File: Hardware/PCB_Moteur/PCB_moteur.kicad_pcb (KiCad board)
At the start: 2 copper layers, 60 x 113 mm, 191 parts, among them J1 XT30PW-F, J10 Conn_01x02, J11 Conn_01x02, J12 Conn_01x02, J13 Conn_01x02, J14 Conn_01x02, J15 Conn_01x02, J16 Conn_01x06_Pin, J17 Screw_Terminal_01x04, J18 Screw_Terminal_01x04, J19 Screw_Terminal_01x04, J2 Conn_01x06_Pin, J3 Conn_01x03_Socket, J4 Conn_01x03_Socket, J5 Conn_01x03_Socket, J6 Conn_01x03_Socket, J7 Conn_01x02, J8 Conn_01x02, J9 Conn_01x02, Q1 SI5442DU-T1-GE3, Q2 SI5442DU-T1-GE3, Q3 MMBT3904, Q4 SI7617DN-T1-GE3, U1 L6981N33DR, U2 STM32F103CBT6, U3 MCP1802T-5002I/OT, U4 LSF0204PWR, U5 ISOW1044, U6 LM393, U7 INA125UA/2K5, U8 INA125UA/2K5, U9 MAX6612MXK

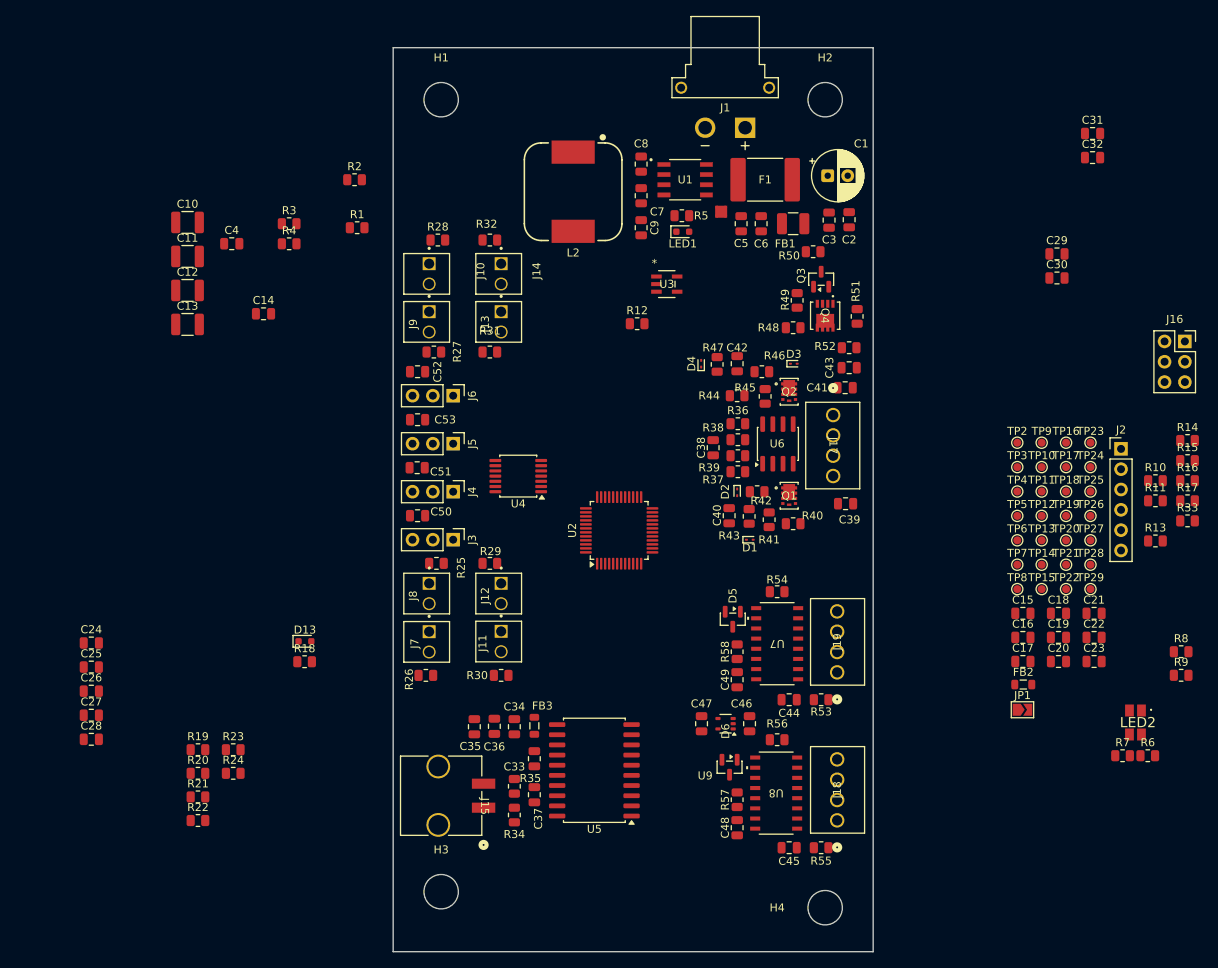
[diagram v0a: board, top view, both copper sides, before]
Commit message: wip: layout presque fini (decoup stm32 restant)
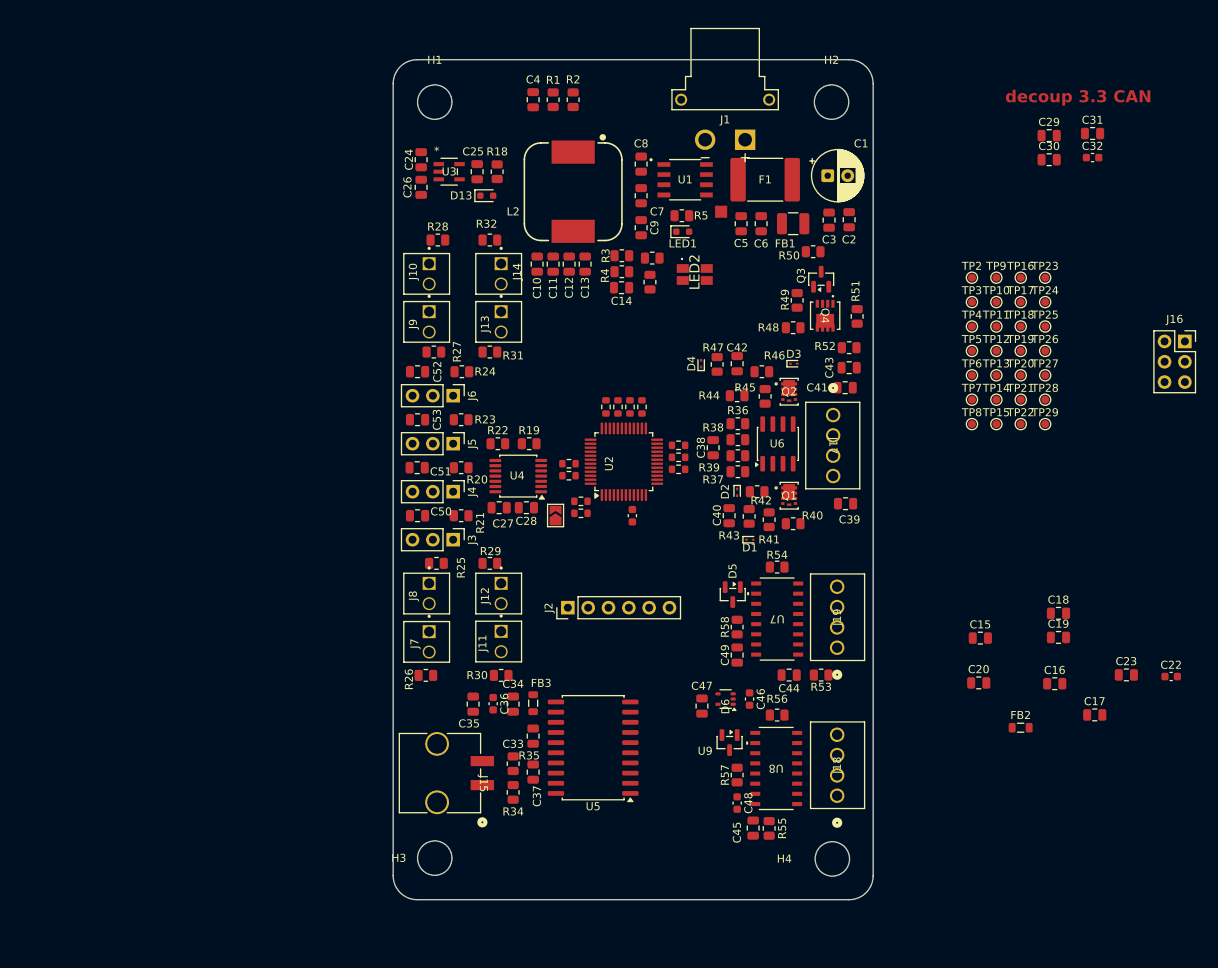
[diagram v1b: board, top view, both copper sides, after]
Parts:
- C10, C11, C12, C13: footprint Capacitor_SMD:C_1210_3225Metric -> Capacitor_SMD:C_0805_2012Metric
- C21, C22, C32, C36, C46, C48: footprint Capacitor_SMD:C_0805_2012Metric -> Capacitor_SMD:C_0603_1608Metric
- R10, R11, R12, R13, R14, R15, R16, R17, R33, R8, R9: footprint Resistor_SMD:R_0805_2012Metric -> Resistor_SMD:R_0603_1608Metric
- moved R6 87.8 mm to (115.4, 59.3)
- moved R7 83.6 mm to (115.1, 62.3), turned to 90 degrees
- moved LED2 78.6 mm to (120.7, 61.4), turned to 90 degrees
- moved C25 78.5 mm to (93.5, 48.5), turned to -90 degrees
- moved R9 78.1 mm to (106.5, 89.7)
- moved R33 77.6 mm to (105.0, 85.0)
- moved R8 77.0 mm to (106.5, 91.2), turned to 180 degrees
- moved C26 75.3 mm to (86.5, 50.5), turned to 90 degrees
- moved R13 73.8 mm to (105.0, 86.5)
- moved R17 73.6 mm to (109.6, 77.9), turned to 90 degrees
- moved C24 73.1 mm to (86.5, 47.0), turned to -90 degrees
- moved J2 71.9 mm to (104.8, 103.0), turned to 90 degrees
- moved R16 71.8 mm to (111.1, 77.9), turned to 90 degrees
- moved R15 70.0 mm to (112.6, 77.9), turned to 90 degrees
- moved R14 68.3 mm to (114.1, 77.9), turned to 90 degrees
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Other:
- board size 60 x 113 mm -> 60 x 105 mm
- board text added: "decoup 3.3 CAN"

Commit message: wip: nouveaux connecteurs et espace pour ceux-ci
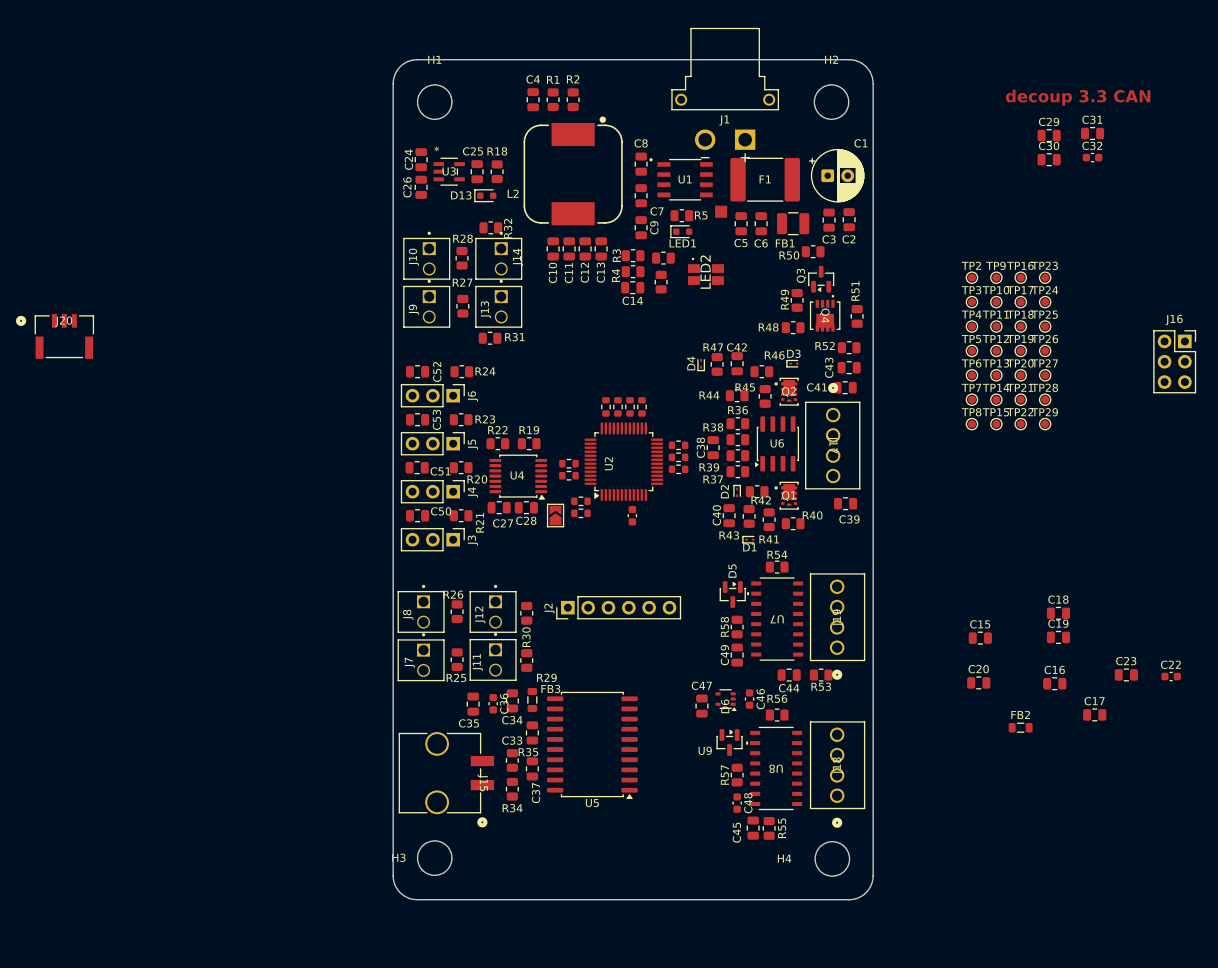
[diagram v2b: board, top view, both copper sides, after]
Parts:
- added J20: BM03B-GHS-TBT, pcb_moteur:CONN_BM03B-GHS-TBT_JST, F.Cu at (41.9, 69.1)
- moved R29 13.0 mm to (99.7, 109.6), turned to -90 degrees
- moved R25 12.3 mm to (91.0, 109.5), turned to -90 degrees
- moved R26 8.87 mm to (91.0, 103.5), turned to -90 degrees
- moved R30 8.39 mm to (99.7, 103.7), turned to -90 degrees
- moved R27 6.77 mm to (91.7, 65.3), turned to -90 degrees
- moved R28 3.78 mm to (91.6, 59.3), turned to -90 degrees
- moved C10 2.76 mm to (103.0, 58.1)
- moved C11 2.76 mm to (105.0, 58.1)
- moved C12 2.76 mm to (107.0, 58.1)
- moved C13 2.76 mm to (109.0, 58.1)
- moved J11 2.40 mm to (95.8, 108.3)
- moved J12 2.40 mm to (95.8, 102.3)
- moved J8 2.40 mm to (86.8, 102.3)
- moved J7 2.40 mm to (86.8, 108.3)
- moved L2 2.20 mm to (105.5, 48.8)
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
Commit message: wip: arrangement connecteurs et modeles 3D
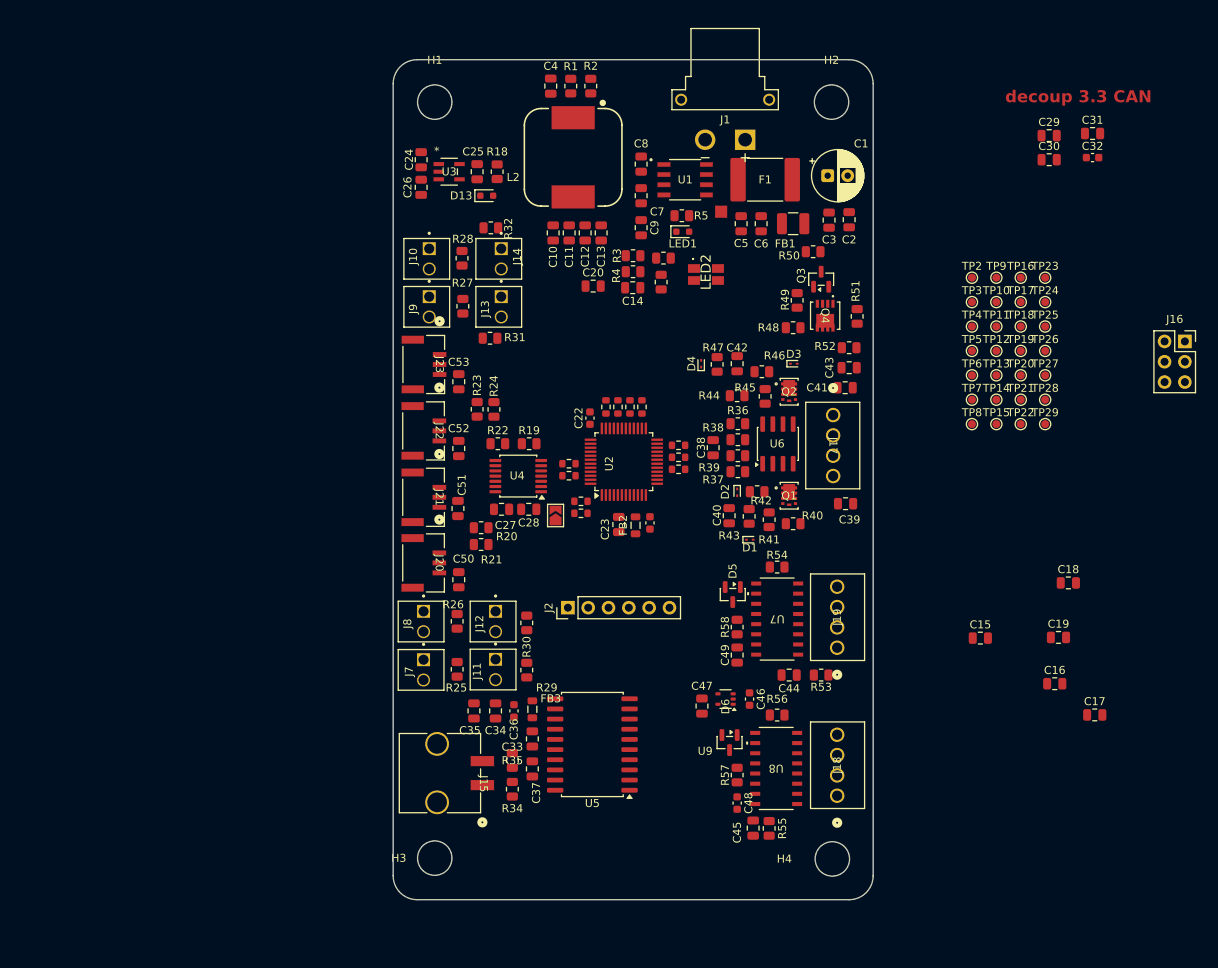
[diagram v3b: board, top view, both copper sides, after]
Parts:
- removed J3, J4, J5, J6: Conn_01x03_Socket, Connector_PinHeader_2.54mm:PinHeader_1x03_P2.54mm_Vertical
- added J21: BM03B-GHS-TBT, pcb_moteur:CONN_BM03B-GHS-TBT_JST, F.Cu at (86.8, 89.2)
- added J22: BM03B-GHS-TBT, pcb_moteur:CONN_BM03B-GHS-TBT_JST, F.Cu at (86.8, 80.9)
- added J23: BM03B-GHS-TBT, pcb_moteur:CONN_BM03B-GHS-TBT_JST, F.Cu at (86.8, 72.6)
- moved C22 79.5 mm to (107.6, 79.3), turned to -90 degrees
- moved C20 69.2 mm to (108.0, 62.8)
- moved C23 66.2 mm to (111.2, 92.6), turned to -90 degrees
- moved FB2 54.4 mm to (113.3, 92.7), turned to 90 degrees
- moved J20 53.1 mm to (86.8, 97.4), turned to -90 degrees
- moved C52 10.9 mm to (91.2, 83.1), turned to -90 degrees
- moved C50 9.51 mm to (91.2, 99.5), turned to -90 degrees
- moved R20 7.91 mm to (94.0, 93.0)
- moved C51 7.21 mm to (91.1, 90.6), turned to -90 degrees
- moved C53 7.01 mm to (91.2, 74.8), turned to -90 degrees
- moved R24 6.19 mm to (95.6, 78.2), turned to 90 degrees
- moved R21 4.38 mm to (94.0, 95.1)
- moved C18 4.00 mm to (167.4, 99.9)
- moved C4 2.78 mm to (102.7, 37.8)
- moved R1 2.78 mm to (105.2, 37.8)
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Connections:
- J20 pad 1: unconnected-(J20-Pad1) -> Servo1_Stepup
- J20 pad 2: unconnected-(J20-Pad2) -> VIN_Filtered
- J20 pad 3: unconnected-(J20-Pad3) -> LC_IN-

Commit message: wip: finis layout, DRIP MAXIMALE
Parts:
- added G***: LOGO, LOGO, B.Cu at (114.6, 85.9)
- moved C31 97.3 mm to (117.3, 125.3), turned to 90 degrees
- moved C32 96.1 mm to (115.1, 125.3), turned to 90 degrees
- moved C30 82.9 mm to (114.0, 112.3), turned to 180 degrees
- moved J16 79.5 mm to (110.7, 105.0), turned to 90 degrees
- moved C29 78.6 mm to (119.2, 107.9), turned to -90 degrees
- moved C19 66.9 mm to (105.2, 79.1), turned to -90 degrees
- moved C17 66.1 mm to (117.5, 77.2), turned to 180 degrees
- moved C15 64.6 mm to (105.5, 67.1), turned to 90 degrees
- moved C18 61.0 mm to (106.7, 93.5), turned to 180 degrees
- moved C16 58.0 mm to (117.5, 80.4), turned to 180 degrees
- moved C20 33.8 mm to (115.4, 95.8), turned to 90 degrees
- moved TP10 16.3 mm to (173.9, 69.7)
- moved TP11 16.3 mm to (173.9, 72.8)
- moved TP14 16.3 mm to (173.9, 81.9)
- moved TP15 16.3 mm to (173.9, 85.0)
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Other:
- board text removed: "decoup 3.3 CAN"

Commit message: wip: début routing
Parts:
- C48: value 10nF -> 100nF; footprint Capacitor_SMD:C_0603_1608Metric -> Capacitor_SMD:C_0805_2012Metric
- C49: value 10nF -> 100nF
- moved J2 29.3 mm to (113.9, 71.9), turned to -90 degrees
- moved C48 13.9 mm to (129.8, 114.0), turned to 0 degrees
- moved R53 7.42 mm to (129.1, 110.7)
- moved R57 7.14 mm to (127.0, 116.8), turned to 0 degrees
- moved U9 6.75 mm to (125.2, 107.7), turned to -90 degrees
- moved C47 6.73 mm to (122.7, 108.7)
- moved C49 5.69 mm to (121.9, 105.0), turned to 0 degrees
- moved C29 5.46 mm to (117.1, 112.9)
- moved C45 5.20 mm to (133.0, 129.2), turned to 180 degrees
- moved C46 4.90 mm to (125.3, 110.1), turned to 0 degrees
- moved R58 4.81 mm to (121.9, 102.9), turned to 180 degrees
- moved R55 1.43 mm to (129.5, 129.2), turned to 0 degrees
- moved C44 0.75 mm to (132.6, 110.7)
- moved C20 0.71 mm to (115.5, 96.4)
- moved C23 0.66 mm to (110.8, 93.2)
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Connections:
- U7 pad 10: Net-(U7-SENSE) -> Net-(D5-COM)
- U7 pad 11: Net-(U7-SENSE) -> Net-(D5-COM)
- U8 pad 10: Net-(U8-SENSE) -> Net-(D6-COM)
- U8 pad 11: Net-(U8-SENSE) -> Net-(D6-COM)
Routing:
- net LCell_Sleep: track 0.00 -> 49.7 mm
- net Pressure_Sleep: track 0.00 -> 42.1 mm
- net LCell_An: track 0.00 -> 39.7 mm
- net LC_IN+: track 0.00 -> 24.5 mm
- net P_IN+: track 0.00 -> 24.0 mm
- net Pressure_An: track 0.00 -> 20.6 mm
- net Net-(D6-COM): track 0.00 -> 7.53 mm
- net Net-(D5-COM): track 0.00 -> 7.02 mm
- net LC_OUT-: track 0.00 -> 5.43 mm
- net P_OUT-: track 0.00 -> 5.24 mm
- net LC_OUT+: track 0.00 -> 5.10 mm
- net P_OUT+: track 0.00 -> 5.05 mm
- net Temp_An: track 0.00 -> 3.77 mm
- net Net-(R56-Pad1): track 0.00 -> 2.99 mm
- net Net-(R56-Pad2): track 0.00 -> 2.89 mm
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
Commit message: wip: routing (suite)
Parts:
- moved C47 11.4 mm to (120.7, 97.4)
- moved C46 11.4 mm to (123.3, 98.8)
- moved U9 11.4 mm to (123.2, 96.4)
- moved J16 5.26 mm to (106.5, 101.8)
- moved C30 3.11 mm to (116.4, 114.2), turned to 90 degrees
- moved JP1 2.79 mm to (104.7, 93.9)
- moved U4 2.42 mm to (96.4, 85.6)
- moved C29 2.40 mm to (119.0, 114.3), turned to 90 degrees
- moved C27 2.05 mm to (94.5, 90.6)
- moved R19 2.00 mm to (98.2, 81.7)
- moved C28 1.82 mm to (98.1, 90.5)
- moved R22 1.64 mm to (94.7, 81.7)
- moved C37 0.82 mm to (100.0, 123.9)
- moved R13 0.64 mm to (104.9, 87.1)
- moved C18 0.54 mm to (107.0, 93.9), turned to 90 degrees
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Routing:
- net ISO_CAN_RXD: track 0.00 -> 49.7 mm
- net ISO_CAN_IN: track 0.00 -> 45.2 mm
- net Servo1_Open: track 0.00 -> 44.1 mm
- net ISO_CAN_TXD: track 0.00 -> 38.4 mm
- net Servo1_Close: track 0.00 -> 35.4 mm
- net Servo2_Close: track 0.00 -> 25.9 mm
- net EXTEND_IO1: track 0.00 -> 24.3 mm, vias 0 -> 2
- net EXTEND_IO3: track 0.00 -> 16.8 mm
- net EXTEND_IO4: track 0.00 -> 14.1 mm
- net EXTEND_IO2: track 0.00 -> 13.5 mm
- net Temp_An: track 3.77 -> 14.5 mm
- net Net-(J15-Pin_1): track 0.00 -> 10.5 mm
- net Net-(J15-Pin_2): track 0.00 -> 10.2 mm
- net BOOT0: track 0.00 -> 8.96 mm
- net LCell_Sleep: track 49.7 -> 56.5 mm
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
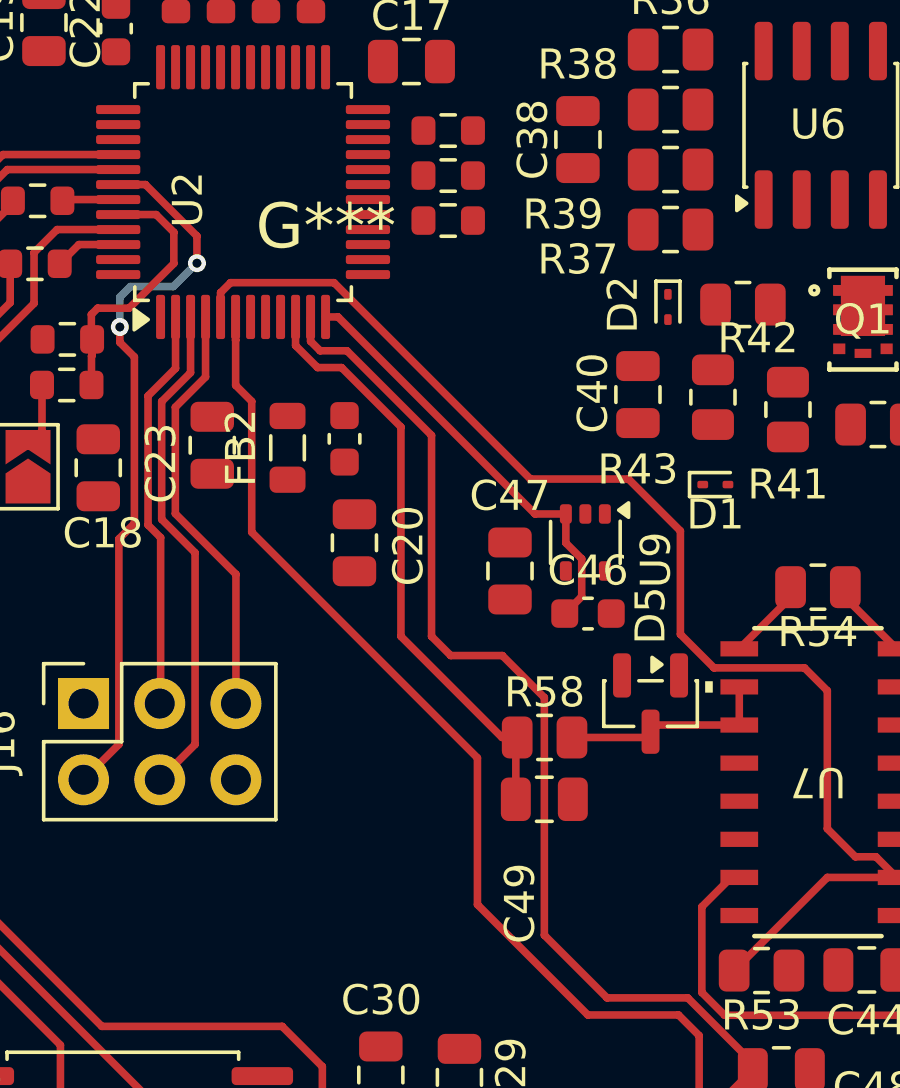
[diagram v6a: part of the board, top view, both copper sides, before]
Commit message: feat: copy all existing schematics in gse project + add missing components + fix voltage divider for 3S + create gse project and seperate stm32 project + add missing resistors motor
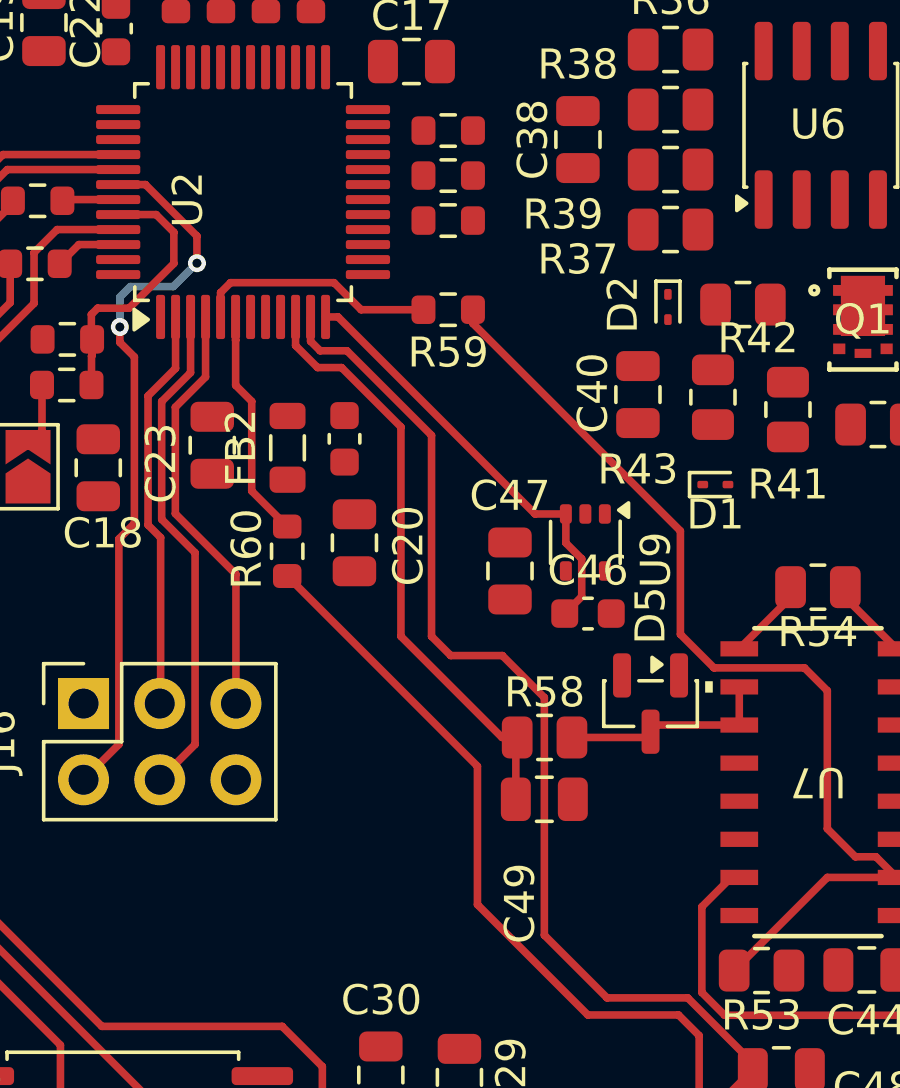
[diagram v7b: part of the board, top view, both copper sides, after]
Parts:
- added R59: 22R, Resistor_SMD:R_0603_1608Metric, F.Cu at (118.7, 88.7)
- added R60: 22R, Resistor_SMD:R_0603_1608Metric, F.Cu at (113.3, 96.7)
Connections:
- net Net-(J15-Pin_1) renamed /Interfaces/CAN+
- net Net-(J15-Pin_2) renamed /Interfaces/CAN-
- U2 pad 5: Pressure_Sleep -> Net-(U2-PD0)
- U2 pad 6: LCell_Sleep -> Net-(U2-PD1)
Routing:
- net Pressure_Sleep: track 43.1 -> 33.6 mm
- net LCell_Sleep: track 56.5 -> 47.1 mm
- net Net-(U2-PD0): track 0.00 -> 8.08 mm
- net Net-(U2-PD1): track 0.00 -> 7.70 mm
